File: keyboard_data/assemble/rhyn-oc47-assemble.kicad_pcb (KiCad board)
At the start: 2 copper layers, 228.8 x 76.2 mm, 97 parts, among them SW1 SW_PUSH, SW10 SW_PUSH, SW11 SW_PUSH, SW12 SW_PUSH, SW13 SW_PUSH, SW14 SW_PUSH, SW15 SW_PUSH, SW16 SW_PUSH, SW17 SW_PUSH, SW18 SW_PUSH, SW19 SW_PUSH, SW2 SW_PUSH, SW20 SW_PUSH, SW21 SW_PUSH, SW22 SW_PUSH, SW23 SW_PUSH, SW24 SW_PUSH, SW25 SW_PUSH, SW26 SW_PUSH, SW27 SW_PUSH, SW28 SW_PUSH, SW29 SW_PUSH, SW3 SW_PUSH, SW30 SW_PUSH, SW31 SW_PUSH, SW32 SW_PUSH, SW33 SW_PUSH, SW34 SW_PUSH, SW35 SW_PUSH, SW36 SW_PUSH, SW37 SW_PUSH, SW38 SW_PUSH, SW39 SW_PUSH, SW4 SW_PUSH, SW40 SW_PUSH, SW41 SW_PUSH, SW42 SW_PUSH, SW43 SW_PUSH, SW44 SW_PUSH, SW45 SW_PUSH, SW46 SW_PUSH, SW47 SW_PUSH, SW5 SW_PUSH, SW6 SW_PUSH, SW7 SW_PUSH, SW8 SW_PUSH, SW9 SW_PUSH, U2 RP2040-Tiny

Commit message: fix: fix the typo and adjust the size of the silkscreen in the bottom right corner
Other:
- board text added: "RHYn-OC47 v0.1 designed by ryoo.cc"
- board text removed: "RHYn-OC47 v0.1 designd by ryoo.cc"

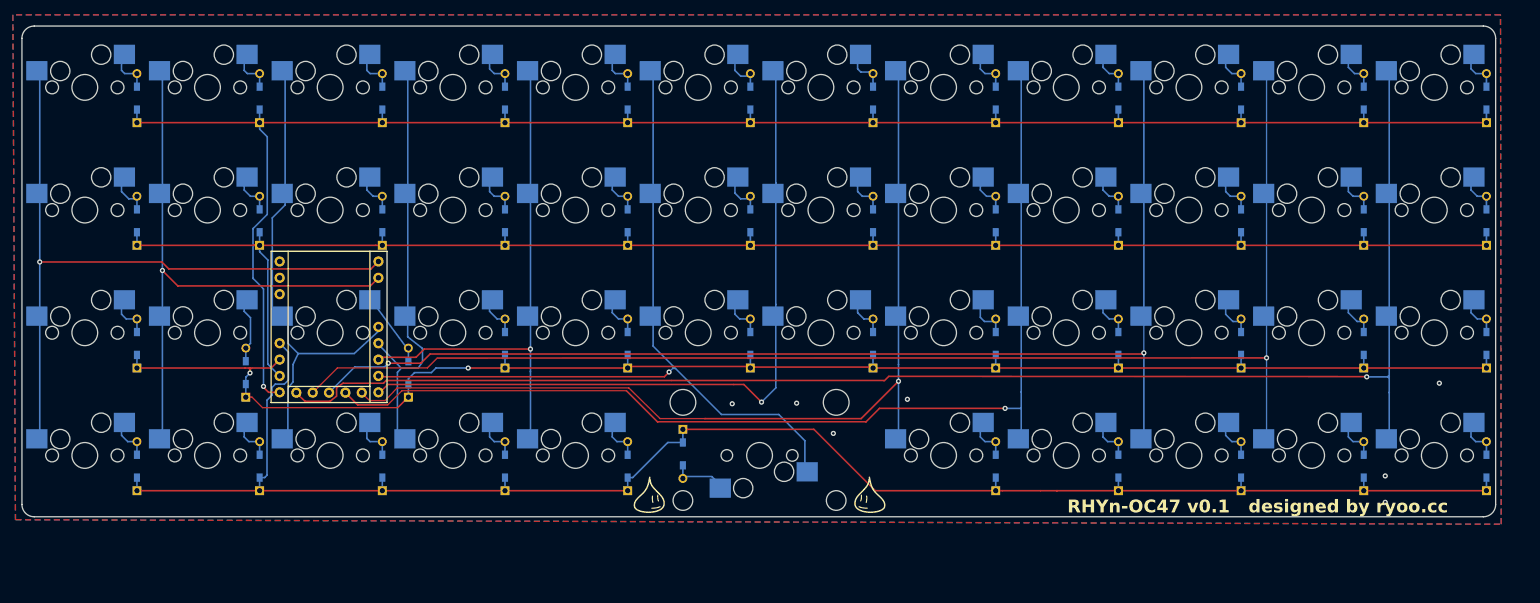
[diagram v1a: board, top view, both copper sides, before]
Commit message: chore: clean up routing and add edge vias
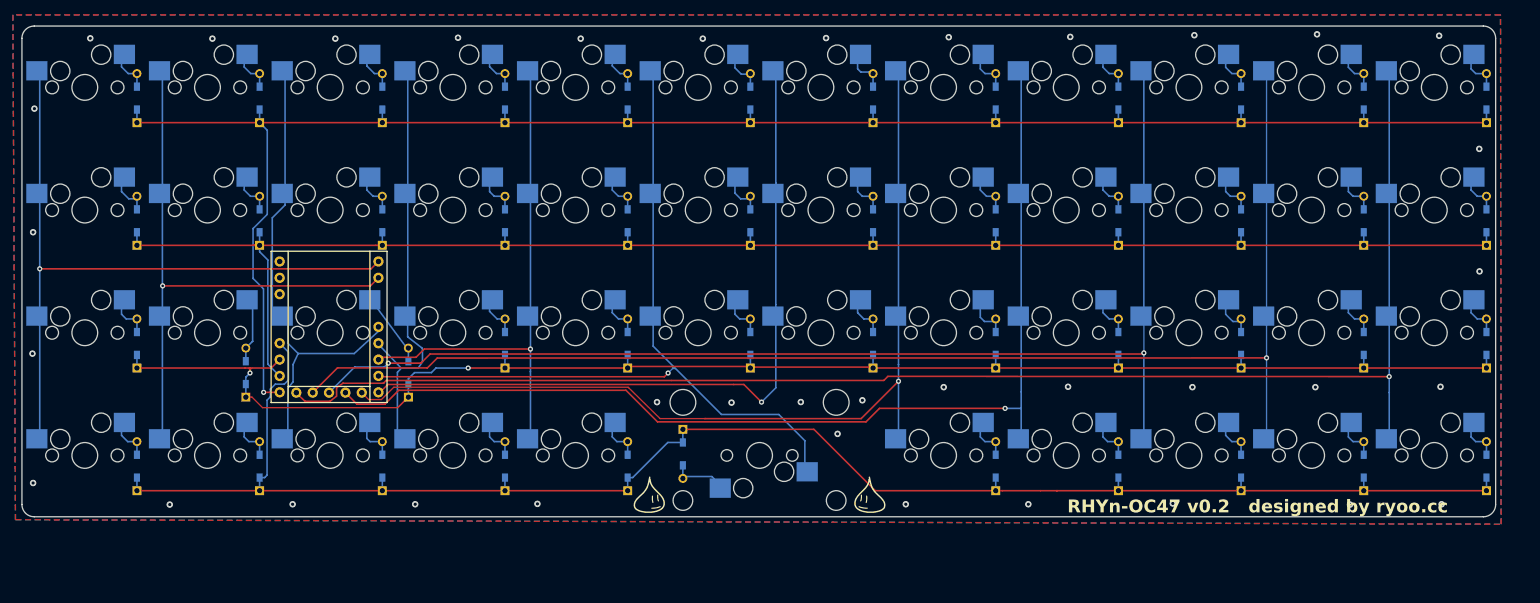
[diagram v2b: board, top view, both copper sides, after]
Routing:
- net Col7: track 89.7 -> 132.4 mm
- net Col11: track 60.6 -> 57.2 mm
- net Col8: track 163.5 -> 166.6 mm
- net Col1: track 92.2 -> 91.2 mm
- net Net-(D35-A): track 7.01 -> 6.44 mm
- net Col0: track 110.7 -> 110.2 mm
- net GND: vias 7 -> 37
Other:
- board text added: "RHYn-OC47 v0.2 designed by ryoo.cc"
- board text removed: "RHYn-OC47 v0.1 designed by ryoo.cc"

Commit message: fix: avoid orthogonal traces through vias
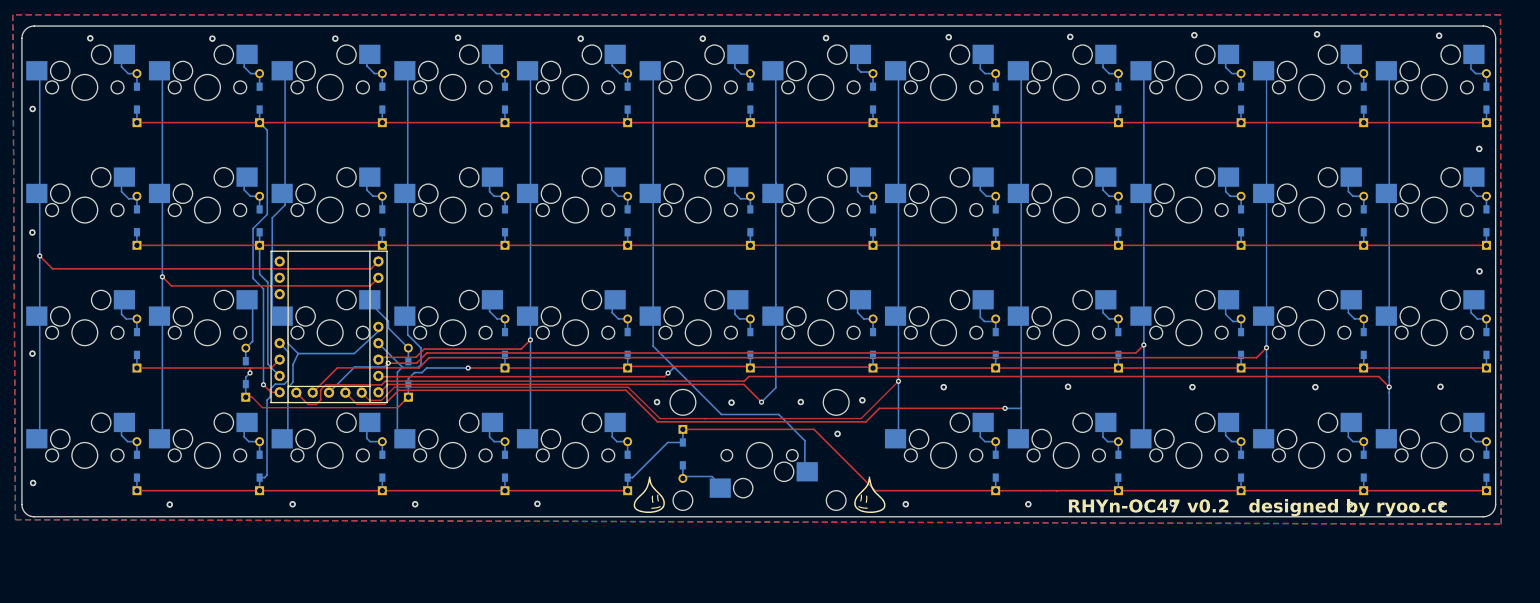
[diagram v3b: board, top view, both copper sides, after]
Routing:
- net Col11: track 57.2 -> 231.0 mm
- net Col10: track 78.8 -> 208.2 mm
- net Col3: track 38.1 -> 54.8 mm
- net Net-(D27-A): track 2.03 -> 12.2 mm
- net Col9: track 180.5 -> 186.7 mm
- net Col5: track 83.2 -> 84.2 mm
- net Col0: track 110.2 -> 111.0 mm
- net Row0: track 280.4 -> 279.7 mm
- net Col4: track 80.9 -> 81.5 mm
- net Col1: track 91.2 -> 91.8 mm

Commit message: feat: rewire myself
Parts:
- U2: moved to B.Cu
- moved U2 79.0 mm to (169.3, 72.9), turned to 180 degrees
- moved D19 14.0 mm to (190.1, 80.8), turned to 0 degrees
- moved D18 7.51 mm to (153.9, 81.7), turned to 0 degrees
- moved D27 6.02 mm to (101.2, 94.4)
- moved D26 5.26 mm to (82.0, 94.3)
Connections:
- U2 pad 0: Col0 -> Row0
- U2 pad 1: Col1 -> Row1
- U2 pad 10: Col8 -> Col1
- U2 pad 11: Col9 -> Col2
- U2 pad 12: Col10 -> Col3
- U2 pad 13: Col11 -> Col4
- U2 pad 14: Row0 -> Col11
- U2 pad 15: Row1 -> Col10
- U2 pad 26: Row2 -> Col9
- U2 pad 27: Row3 -> Col8
- U2 pad 5: Col3 -> Col5
- U2 pad 6: Col4 -> Col6
- U2 pad 7: Col5 -> Row3
- U2 pad 8: Col6 -> Row2
- U2 pad 9: Col7 -> Col0
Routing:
- net Col2: track 41.0 -> 158.9 mm, vias 0 -> 2
- net Col11: track 231.0 -> 138.7 mm
- net Col10: track 208.2 -> 120.6 mm
- net Col0: track 111.0 -> 198.5 mm
- net Col3: track 54.8 -> 141.6 mm, vias 0 -> 2
- net Col1: track 91.8 -> 178.1 mm, vias 1 -> 2
- net Col9: track 186.7 -> 104.2 mm
- net Col6: track 115.1 -> 41.5 mm, vias 1 -> 0
- net Row2: track 199.3 -> 266.4 mm, vias 2 -> 0
- net Col8: track 166.6 -> 103.9 mm, vias 1 -> 2
- net Col4: track 81.5 -> 138.1 mm, vias 1 -> 2
- net Col7: track 132.5 -> 80.9 mm, vias 1 -> 2
- net Row0: track 279.7 -> 239.5 mm, vias 1 -> 0
- net Row3: track 262.7 -> 296.3 mm, vias 0 -> 2
- net Col5: track 84.2 -> 113.1 mm, vias 1 -> 0
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- removed copper zone on B.Cu, net GND
- removed copper zone on F.Cu, net GND

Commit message: chore: gnd beta
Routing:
- net GND: vias 0 -> 20
- net (no net): vias 0 -> 23
- added copper zone on B.Cu, net GND
- added copper zone on F.Cu, net GND

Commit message: chore: add big icon
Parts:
- added G***: LOGO, ucib:ryoo_big_icon, B.Cu at (90.1, 83.6)
- added G***: LOGO, ucib:ryoo_big_icon, B.Cu at (235.3, 83.9)
- added G***: LOGO, ucib:ryoo_big_icon, B.Cu at (160.8, 84.6)
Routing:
- net GND: vias 20 -> 28
- net (no net): vias 23 -> 24

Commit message: chore: change icons
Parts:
- removed the G*** at (176.7, 118.1)
- removed the G*** at (142.4, 118.1)
- removed the G*** at (90.1, 83.6)
- removed the G*** at (235.3, 83.9)
- removed the G*** at (160.8, 84.6)
- added G***: LOGO, rhyn-ow:clikclak_icon_1cm, F.Cu at (178.6, 116.8)
- added G***: LOGO, rhyn-ow:ryoo_icon_1cm, F.Cu at (142.1, 117.0)
